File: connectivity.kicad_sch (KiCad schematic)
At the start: 21 parts, among them J11 RJ45_Hanrun_HR911105A_Horizon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, U5 LAN8742A, Y3 25 MHz

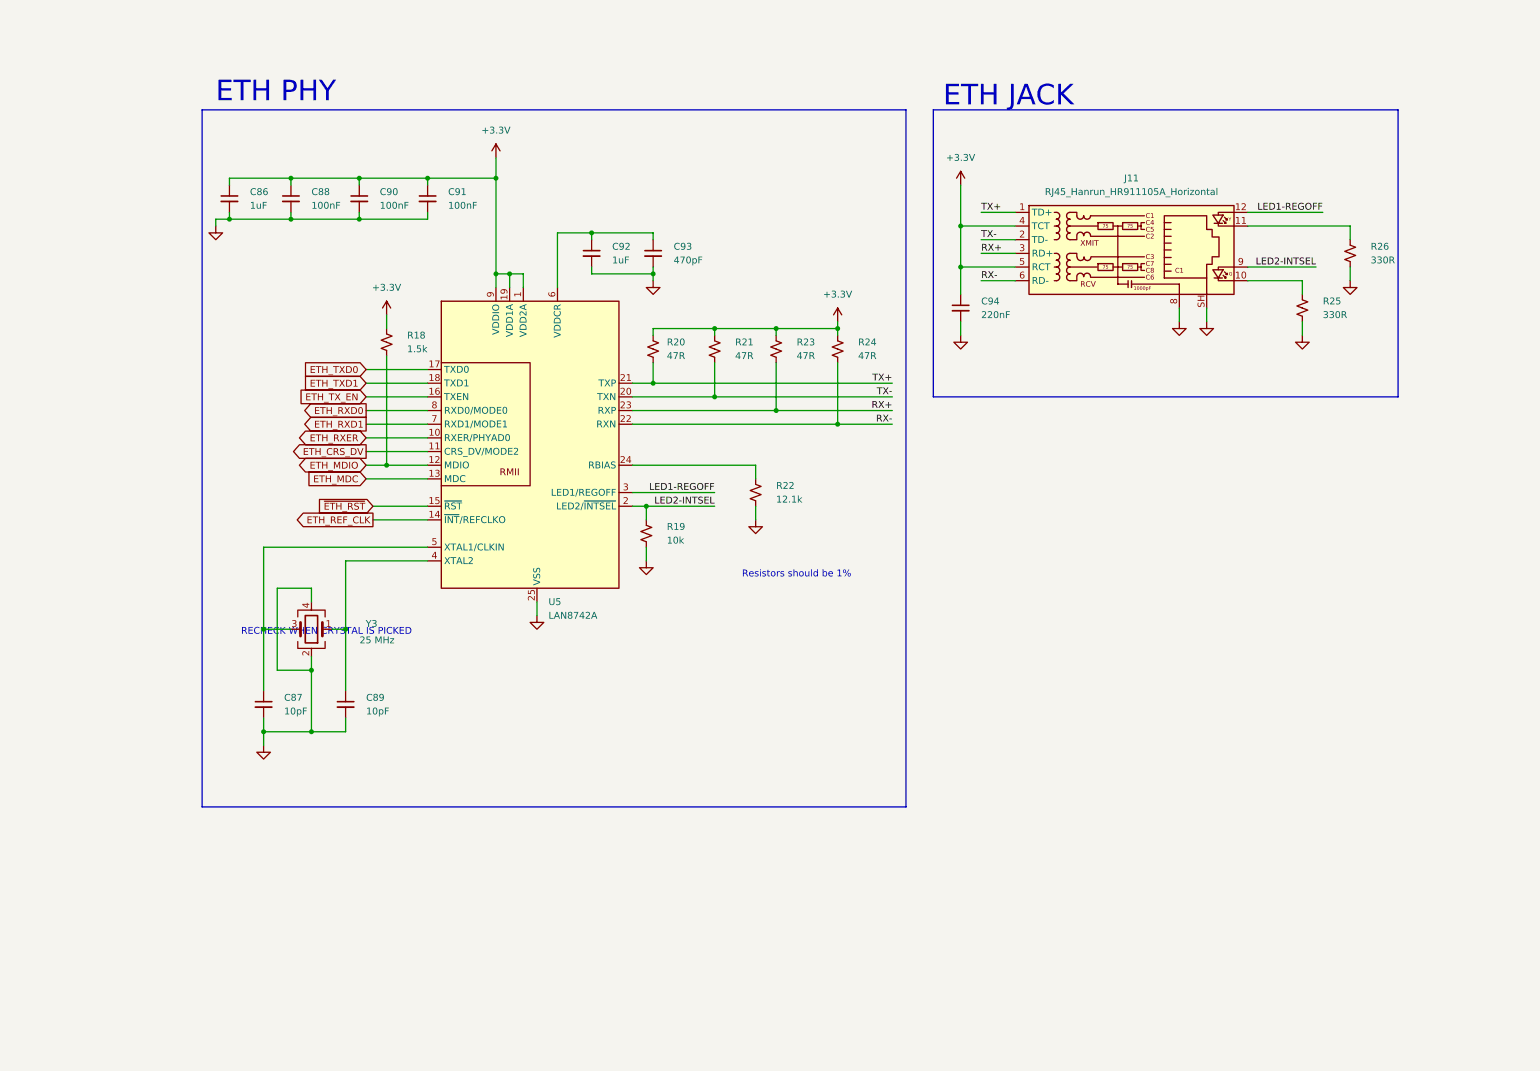
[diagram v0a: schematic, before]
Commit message: Soften scope, begin layout, reorganize sheets (still need to delete extras)
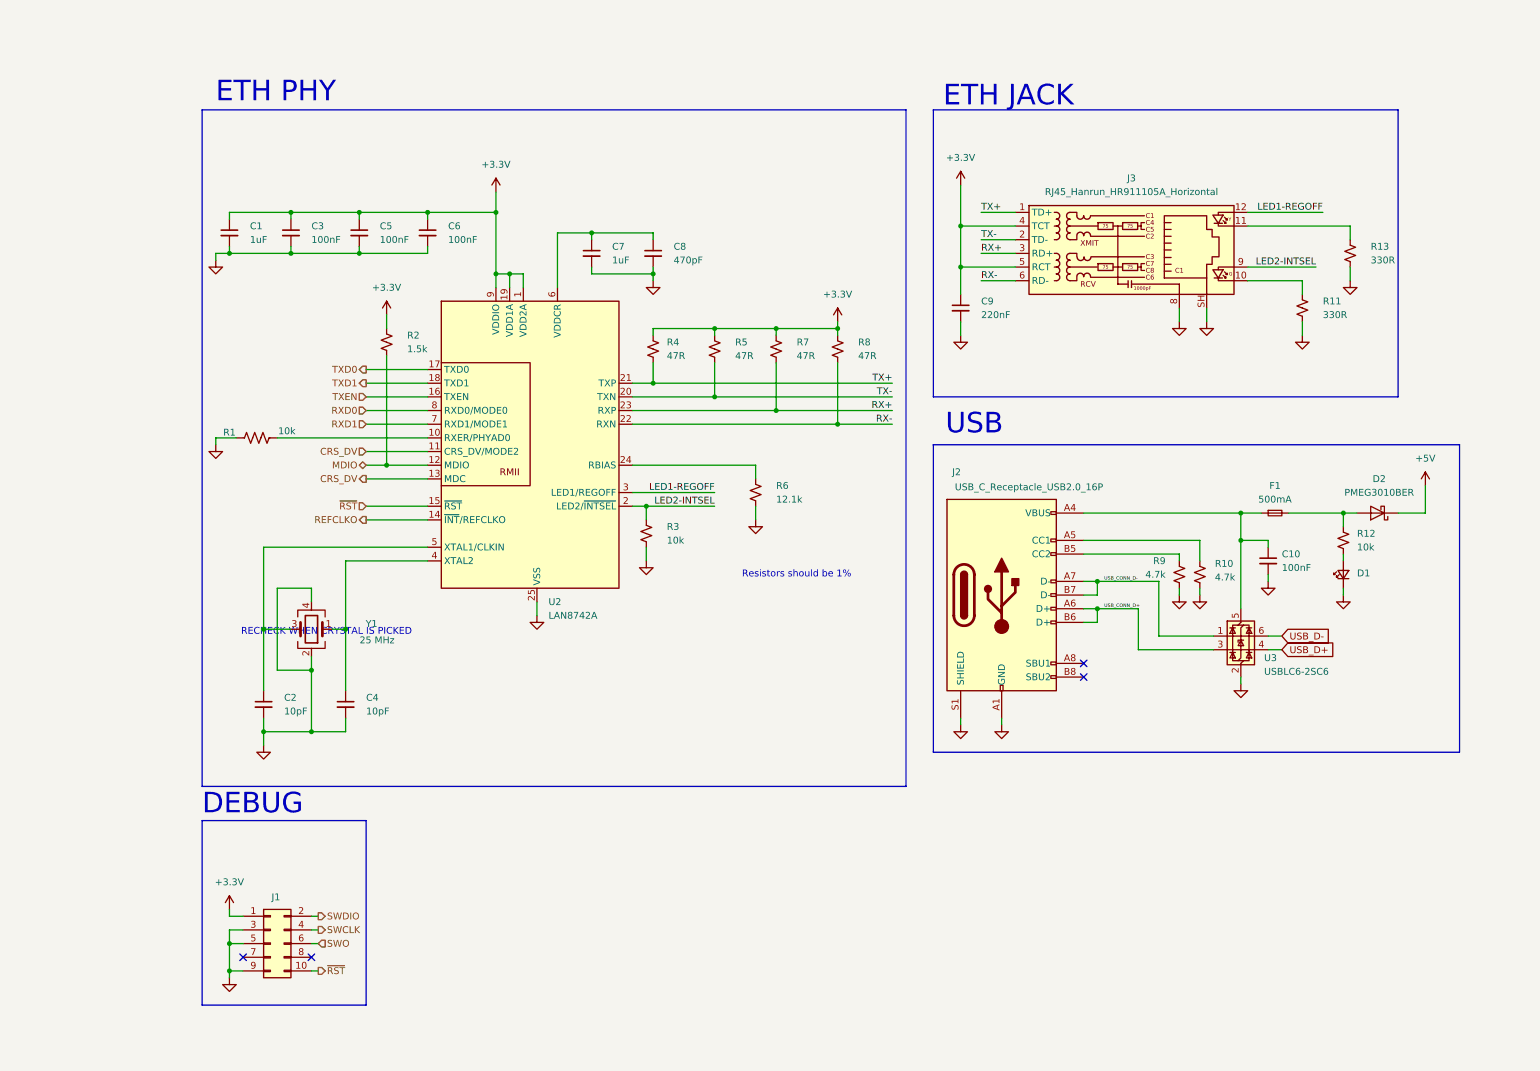
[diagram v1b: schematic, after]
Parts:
- added C10: 100nF, APRLPrints:C_0603, symbol Device:C_Small
- added D1: LED_Small, APRLPrints:LED_0603, symbol Device:LED_Small
- added D2: PMEG3010BER, Diode_SMD:Nexperia_CFP3_SOD-123W, symbol Diode:PMEG3010BER
- added F1: 500mA, Fuse:Fuse_0805_2012Metric, symbol Device:Fuse_Small
- added J1: Conn_02x05_Odd_Even, Connector_PinHeader_2.54mm:PinHeader_1x10_P2.54mm_Vertical, symbol Connector_Generic:Conn_02x05_Odd_Even
- added J2: USB_C_Receptacle_USB2.0_16P, Connector_USB:USB_C_Receptacle_HRO_TYPE-C-31-M-12, symbol Connector:USB_C_Receptacle_USB2.0_16P
- added R1: 10k, APRLPrints:R_0603, symbol Device:R_US
- added R10, R9: 4.7k, APRLPrints:R_0603, symbol Device:R_Small_US
- added R12: 10k, APRLPrints:R_0603, symbol Device:R_Small_US
- added U3: USBLC6-2SC6, Package_TO_SOT_SMD:SOT-23-6, symbol Power_Protection:USBLC6-2SC6
- C1: renamed from C86; footprint aprlprints:C_0603-noct -> APRLPrints:C_0603; LCSC C602037 -> (none)
- C2: renamed from C87; footprint aprlprints:C_0603-noct -> APRLPrints:C_0603; LCSC C32949 -> (none)
- C3: renamed from C88; footprint aprlprints:C_0603-noct -> APRLPrints:C_0603; LCSC C1525 -> (none)
- C4: renamed from C89; footprint aprlprints:C_0603-noct -> APRLPrints:C_0603; LCSC C32949 -> (none)
- C5: renamed from C90; footprint aprlprints:C_0603-noct -> APRLPrints:C_0603; LCSC C1525 -> (none)
- C6: renamed from C91; footprint aprlprints:C_0603-noct -> APRLPrints:C_0603; LCSC C1525 -> (none)
- C7: renamed from C92; footprint aprlprints:C_0603-noct -> APRLPrints:C_0603; LCSC C602037 -> (none)
- C8: renamed from C93; footprint aprlprints:C_0603-noct -> APRLPrints:C_0603; LCSC C602037 -> (none)
- C9: renamed from C94; footprint aprlprints:C_0603-noct -> APRLPrints:C_0603; LCSC C1525 -> (none)
- J3: renamed from J11; LCSC C12074 -> (none)
- R11: renamed from R25; footprint aprlprints:R_0603-noct -> APRLPrints:R_0603; LCSC C105875 -> (none)
- R13: renamed from R26; footprint aprlprints:R_0603-noct -> APRLPrints:R_0603; LCSC C105875 -> (none)
- R2: renamed from R18; footprint aprlprints:R_0603-noct -> APRLPrints:R_0603; LCSC C60490 -> (none)
- R3: renamed from R19; footprint aprlprints:R_0603-noct -> APRLPrints:R_0603; LCSC C60490 -> (none)
- R4: renamed from R20; footprint aprlprints:R_0603-noct -> APRLPrints:R_0603; LCSC C87044 -> (none)
- R5: renamed from R21; footprint aprlprints:R_0603-noct -> APRLPrints:R_0603; LCSC C87044 -> (none)
- R6: renamed from R22; footprint aprlprints:R_0603-noct -> APRLPrints:R_0603; LCSC C25852 -> (none)
- R7: renamed from R23; footprint aprlprints:R_0603-noct -> APRLPrints:R_0603; LCSC C87044 -> (none)
- R8: renamed from R24; footprint aprlprints:R_0603-noct -> APRLPrints:R_0603; LCSC C87044 -> (none)
- Y1: renamed from Y3; footprint aprlprints:3225-4P-L-noct -> APRLPrints:3225-4P-L; LCSC C2901668 -> (none)
- renumbered U5 to U2
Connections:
- net ETH_MDC is gone; now on net CRS_DV: U2.13 (MDC)
- net +3.3V: now also J1.1 (Pin_1)
- net GND: now also C10.2, D1.1 (K), J1.3 (Pin_3), J1.5 (Pin_5), J1.9 (Pin_9), J2.A1 (GND), J2.A12 (GND), J2.B1 (GND), J2.B12 (GND), J2.S1 (SHIELD), R1.1, R10.2, R9.1, U3.2 (GND)
- net ETH_CRS_DV renamed CRS_DV
- net ETH_MDIO renamed MDIO
- net ETH_REF_CLK renamed REFCLKO
- net ETH_RXD0 renamed RXD0
- net ETH_RXD1 renamed RXD1
- net ETH_RXER: no longer names the net of U2.10 (RXER/PHYAD0)
- net ETH_RXER: now also R1.2
- net ETH_TXD0 renamed TXD0
- net ETH_TXD1 renamed TXD1
- net ETH_TX_EN renamed TXEN
- net ~{ETH_RST} renamed ~{RST}
- net ~{RST}: now also J1.10 (Pin_10)
- new net: J2.A5 (CC1), R10.1
- new net: C10.1, F1.1, J2.A4 (VBUS), J2.A9 (VBUS), J2.B4 (VBUS), J2.B9 (VBUS), U3.5 (VBUS)
- new net: J2.B5 (CC2), R9.2
- new net: D2.2 (A), F1.2, R12.1
- new net: D1.2 (A), R12.2
- new net +5V: D2.1 (K)
- new net SWCLK: J1.4 (Pin_4)
- new net SWDIO: J1.2 (Pin_2)
- new net SWO: J1.6 (Pin_6)
- new net USB_CONN_D+: J2.A6 (D+), J2.B6 (D+), U3.3 (I/O2)
- new net USB_CONN_D-: J2.A7 (D-), J2.B7 (D-), U3.1 (I/O1)
- new net USB_D+: U3.4 (I/O2)
- new net USB_D-: U3.6 (I/O1)
- no-connect marks 0 -> 4
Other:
- note added: "DEBUG"
- note added: "USB"
- moved on the sheet: C1, C3, C5, C6

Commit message: ???
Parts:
- removed C1, C7: 1uF, APRLPrints:C_0603, symbol Device:C_Small
- removed C2, C4: 10pF, APRLPrints:C_0603, symbol Device:C_Small
- removed C3, C5, C6: 100nF, APRLPrints:C_0603, symbol Device:C_Small
- removed C8: 470pF, APRLPrints:C_0603, symbol Device:C_Small
- removed C9: 220nF, APRLPrints:C_0603, symbol Device:C_Small
- removed J3: RJ45_Hanrun_HR911105A_Horizontal, Connector_RJ:RJ45_Hanrun_HR911105A_Horizontal, symbol Connector:RJ45_Hanrun_HR911105A_Horizontal
- removed R1: 10k, APRLPrints:R_0603, symbol Device:R_US
- removed R11, R13: 330R, APRLPrints:R_0603, symbol Device:R_Small_US
- removed R2: 1.5k, APRLPrints:R_0603, symbol Device:R_Small_US
- removed R3: 10k, APRLPrints:R_0603, symbol Device:R_Small_US
- removed R4, R5, R7, R8: 47R, APRLPrints:R_0603, symbol Device:R_Small_US
- removed R6: 12.1k, APRLPrints:R_0603, symbol Device:R_Small_US
- removed U2: LAN8742A, Package_DFN_QFN:VQFN-24-1EP_4x4mm_P0.5mm_EP2.5x2.5mm_ThermalVias, symbol libpt:LAN8742A
- removed Y1: 25 MHz, APRLPrints:3225-4P-L, symbol Device:Crystal_GND24
- added C46, C49, C53: 100nF, symbol Device:C_Small
- added C50: 100pF, symbol Device:C_Small
- added J10: Screw_Terminal_01x02, Connector_Phoenix_MSTB:PhoenixContact_MSTBA_2,5_2-G_1x02_P5.00mm_Horizontal, symbol Connector_Generic:Conn_01x02
- added R26, R31: 10k, symbol Device:R_Small_US
- added R32: 10M, symbol Device:R_Small_US
- added R33: 100k, symbol Device:R_Small_US
- added RN1, RN3: 4.7k, Resistor_SMD:R_Array_Convex_4x0603, symbol libserie:R_Pack04_Split_US
- added U14, U15: TLV6742, symbol Device:Opamp_Dual
- added U16: TMUX1101DBV, Package_TO_SOT_SMD:SOT-23-5, symbol Analog_Switch:TMUX1101DBV
- added U23: TMUX1108PW, Package_SO:TSSOP-16_4.4x5mm_P0.65mm, symbol Analog_Switch:TMUX1108PW
- added U25: ADS1220xPW, Package_SO:TSSOP-16_4.4x5mm_P0.65mm, symbol Analog_ADC:ADS1220xPW
- added U26: LDC1612, Package_SON:WSON-12-1EP_4x4mm_P0.5mm_EP2.6x3mm_ThermalVias, symbol Sensor_Proximity:LDC1612
- added U27: ADS1115IDGS, Package_SO:TSSOP-10_3x3mm_P0.5mm, symbol Analog_ADC:ADS1115IDGS
- renumbered C10 to C51, D1 to D13, D2 to D14, F1 to F5, J2 to J17, J1 to J18, R9 to R46, R10 to R47, R12 to R48, U3 to U24
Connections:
- net +3.3V: now also C46.2, C49.2, C53.2, R26.1, U14.8 (V+), U15.8 (V+), U16.5 (V_{DD}), U23.13 (VDD)
- net GND: now also C46.1, C49.1, C53.1, J10.1 (Pin_1), R31.1, U14.4 (V-), U14.5 (+), U15.4 (V-), U16.2, U16.3 (GND), U23.14 (GND), U23.3 (VSS)
- new net: RN1.3 (R3.1), RN1.5 (R4.2), U23.7 (S4)
- new net: RN1.2 (R2.1), RN1.6 (R3.2), U23.6 (S3)
- new net: R33.2, RN3.4 (R4.1), U15.1, U15.5 (+)
- new net: RN3.3 (R3.1), RN3.5 (R4.2), U23.9 (S8)
- new net: RN3.1 (R1.1), RN3.7 (R2.2), U23.11 (S6)
- new net: RN1.4 (R4.1), RN3.8 (R1.2), U23.12 (S5)
- new net: RN3.2 (R2.1), RN3.6 (R3.2), U23.10 (S7)
- new net: R33.1, U15.2 (-)
- new net: R26.2, R31.2, U14.6 (-)
- new net: C50.1, J10.2 (Pin_2), R32.1, U14.2 (-), U16.1
- new net: C50.2, R32.2, U14.1, U15.3 (+)
- new net: RN1.8 (R1.2), U23.4 (S1)
- new net: RN1.1 (R1.1), RN1.7 (R2.2), U23.5 (S2)
- new net: U26.13 (GND), U26.8 (GND)
- new net A0: U23.1 (A0)
- new net A1: U23.16 (A1)
- new net A2: U23.15 (A2)
- new net PIEZO: U15.6 (-), U15.7
- new net TOGGLE: U16.4
- new net vref: U14.3 (+), U14.7, U23.8 (D)
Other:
- note added: "Main Connections Sheet"
- note added: "Piezo"
- note added: "digitally adjustable amp"
- note added: "extra adc inputs"
- note added: "inductive thing"
- note added: "integrator (charge amp)"
- note added: "load cell input"
- note added: "virtual ground"
- note added: "voltage follower to prevent sag"
- note removed: "ETH JACK"
- note removed: "ETH PHY"
- note removed: "RECHECK WHEN CRYSTAL IS PICKED"
- note removed: "Resistors should be 1%"
- moved on the sheet: C51, D13, D14, F5, J17, J18, R46, R47, R48, U24
